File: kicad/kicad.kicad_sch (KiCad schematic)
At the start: 239 parts, among them sw1 Esc, sw10 Z, sw100 N5, sw101 N6, sw102 N2, sw103 N1, sw104 N0, sw105 MPlay, sw106 MFwd, sw107 NSlash, sw108 NStar, sw109 N8, sw11 LCtrl, sw110 N9, sw111 NMinus, sw112 NPlus, sw113 NEnter, sw114 N3, sw115 NPeriod, sw12 LSys, sw13 F2, sw14 F3, sw15 2, sw16 3, sw17 W, sw18 E, sw19 S, sw2 F1, sw20 D, sw21 X, sw22 C, sw23 LAlt, sw24 THome, sw25 F4, sw26 F5, sw27 4, sw28 5, sw29 R, sw3 Tilda, sw30 T, sw31 F, sw32 G, sw33 V, sw34 B, sw35 LSpace, sw36 TLeft, sw37 F6, sw38 F7, sw39 6, sw4 1, sw40 7, sw41 Y, sw42 U, sw43 H, sw44 J, sw45 N, sw46 M, sw47 TUp, sw48 TDown, sw49 F8, sw5 Tab, sw50 F9, sw51 8, sw52 9, sw53 I, sw54 O, sw55 K, sw56 L, sw57 Comma, sw58 Period, sw59 RSpace, sw6 Q, sw60 TRight, sw61 F10, sw62 F11, sw63 0, sw64 Minus, sw65 P, sw66 LBrack, sw67 Semi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

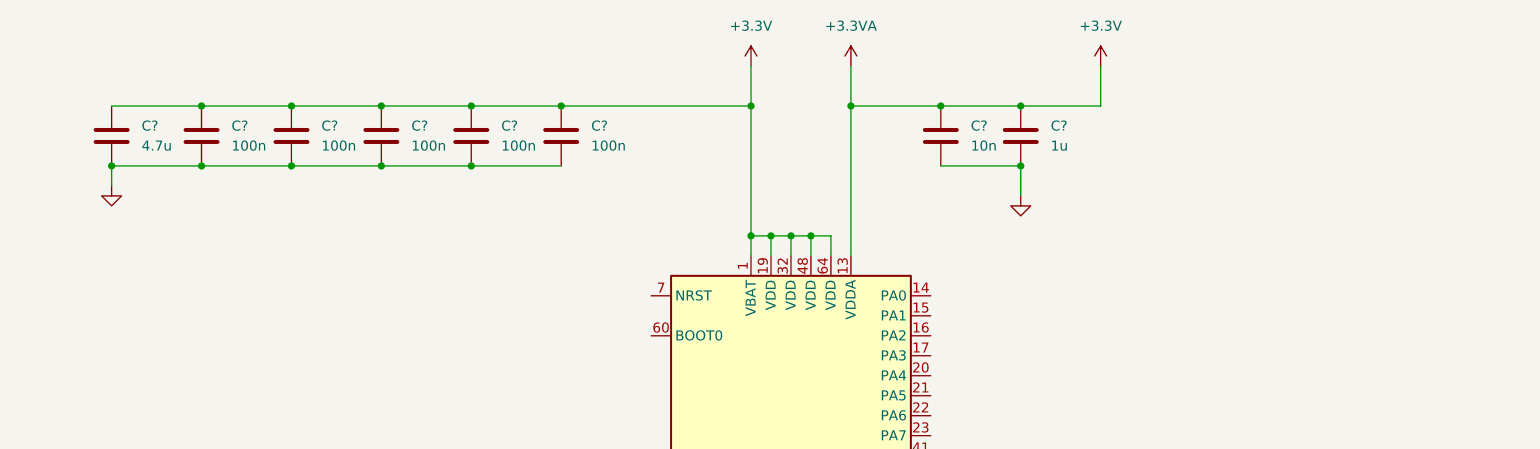
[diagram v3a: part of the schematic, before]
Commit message: Add basic voltage regulator
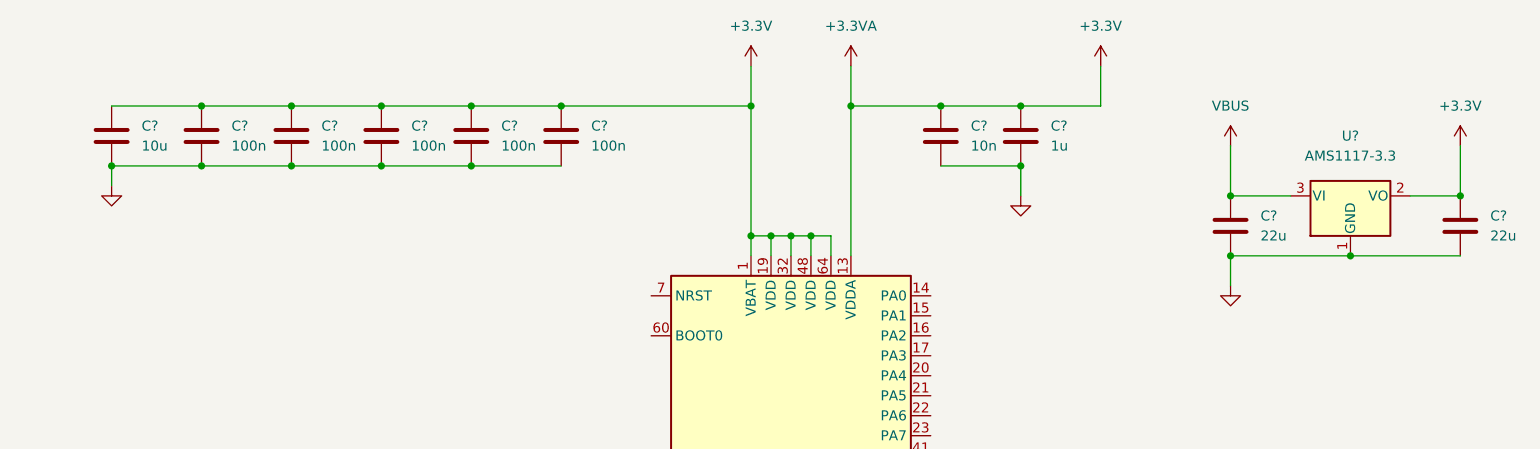
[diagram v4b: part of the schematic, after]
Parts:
- added C? (x2): 22u, symbol Device:C
- added U?: AMS1117-3.3, Package_TO_SOT_SMD:SOT-223-3_TabPin2, symbol Regulator_Linear:AMS1117-3.3
- C?: value 4.7u -> 10u
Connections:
- net +3.3V: now also C?.1, U?.2 (VO)
- net GND: now also C?.2, C?.2, U?.1 (GND)
- new net VBUS: C?.1, U?.3 (VI)
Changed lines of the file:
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@@
   (junction (at 60.96 181.61) (diameter 0) (color 0 0 0 0)
   )
+  (junction (at 397.51 52.07) (diameter 0) (color 0 0 0 0)
+  )
   (junction (at 48.26 166.37) (diameter 0) (color 0 0 0 0)
   )
@@
   (junction (at 49.53 170.18) (diameter 0) (color 0 0 0 0)
   )
+  (junction (at 368.3 52.07) (diameter 0) (color 0 0 0 0)
+  )
   (junction (at 331.47 40.64) (diameter 0) (color 0 0 0 0)
   )
@@
   (junction (at 99.06 90.17) (diameter 0) (color 0 0 0 0)
   )
+  (junction (at 368.3 59.69) (diameter 0) (color 0 0 0 0)
+  )
   (junction (at 151.13 200.66) (diameter 0) (color 0 0 0 0)
   )
@@
   (junction (at 100.33 109.22) (diameter 0) (color 0 0 0 0)
   )
+  (junction (at 383.54 59.69) (diameter 0) (color 0 0 0 0)
+  )
   (junction (at 49.53 33.02) (diameter 0) (color 0 0 0 0)
   )
@@
     (stroke (width 0) (type default) (color 0 0 0 0))
   )
+  (wire (pts (xy 397.51 52.07) (xy 397.51 45.72))
+    (stroke (width 0) (type default) (color 0 0 0 0))
+  )
   (wire (pts (xy 100.33 109.22) (xy 113.03 109.22))
     (stroke (width 0) (type default) (color 0 0 0 0))
@@
     (stroke (width 0) (type default) (color 0 0 0 0))
   )
+  (wire (pts (xy 375.92 52.07) (xy 368.3 52.07))
+    (stroke (width 0) (type default) (color 0 0 0 0))
+  )
   (wire (pts (xy 168.91 63.5) (xy 168.91 101.6))
     (stroke (width 0) (type default) (color 0 0 0 0))
   )
+  (wire (pts (xy 383.54 59.69) (xy 397.51 59.69))
+    (stroke (width 0) (type default) (color 0 0 0 0))
+  )
   (wire (pts (xy 73.66 120.65) (xy 73.66 135.89))
     (stroke (width 0) (type default) (color 0 0 0 0))
@@
     (stroke (width 0) (type default) (color 0 0 0 0))
   )
+  (wire (pts (xy 391.16 52.07) (xy 397.51 52.07))
+    (stroke (width 0) (type default) (color 0 0 0 0))
+  )
   (wire (pts (xy 100.33 196.85) (xy 99.06 196.85))
     (stroke (width 0) (type default) (color 0 0 0 0))
@@
     (stroke (width 0) (type default) (color 0 0 0 0))
   )
+  (wire (pts (xy 368.3 59.69) (xy 383.54 59.69))
+    (stroke (width 0) (type default) (color 0 0 0 0))
+  )
   (wire (pts (xy 87.63 139.7) (xy 87.63 147.32))
     (stroke (width 0) (type default) (color 0 0 0 0))
@@
     (stroke (width 0) (type default) (color 0 0 0 0))
   )
+  (wire (pts (xy 368.3 45.72) (xy 368.3 52.07))
+    (stroke (width 0) (type default) (color 0 0 0 0))
+  )
   (wire (pts (xy 60.96 181.61) (xy 60.96 196.85))
     (stroke (width 0) (type default) (color 0 0 0 0))
@@
     (stroke (width 0) (type default) (color 0 0 0 0))
   )
+  (wire (pts (xy 368.3 59.69) (xy 368.3 63.5))
+    (stroke (width 0) (type default) (color 0 0 0 0))
+  )
   (wire (pts (xy 307.34 40.64) (xy 283.21 40.64))
     (stroke (width 0) (type default) (color 0 0 0 0))
@@
     (pin "2")
   )
+  (symbol (lib_id "Regulator_Linear:AMS1117-3.3") (at 383.54 52.07 0) (unit 1)
+    (in_bom yes) (on_board yes) (fields_autoplaced)
+    (property "Reference" "U?" (id 0) (at 383.54 44.45 0))
+    (property "Value" "AMS1117-3.3" (id 1) (at 383.54 46.99 0))
+    (property "Footprint" "Package_TO_SOT_SMD:SOT-223-3_TabPin2" (id 2) (at 383.54 46.99 0)
+      (effects (font (size 1.27 1.27)) hide)
+    )
+    (property "Datasheet" "http://www.advanced-monolithic.com/pdf/ds1117.pdf" (id 3) (at 386.08 58.42 0)
+      (effects (font (size 1.27 1.27)) hide)
+    )
+    (pin "1")
+    (pin "2")
+    (pin "3")
+  )
   (symbol (lib_id "pspice:DIODE") (at 92.71 74.93 180) (unit 1)
     (in_bom yes) (on_board yes) (fields_autoplaced)
@@
     (pin "2")
   )
+  (symbol (lib_id "power:GND") (at 368.3 63.5 0) (unit 1)
+    (in_bom yes) (on_board yes) (fields_autoplaced)
+    (property "Reference" "#PWR?" (id 0) (at 368.3 69.85 0)
+      (effects (font (size 1.27 1.27)) hide)
+    )
+    (property "Value" "GND" (id 1) (at 368.3 68.58 0)
+      (effects (font (size 1.27 1.27)) hide)
+    )
+    (property "Footprint" "" (id 2) (at 368.3 63.5 0)
+      (effects (font (size 1.27 1.27)) hide)
+    )
+    (property "Datasheet" "" (id 3) (at 368.3 63.5 0)
+      (effects (font (size 1.27 1.27)) hide)
+    )
+    (pin "1")
+  )
   (symbol (lib_id "pspice:DIODE") (at 80.01 166.37 180) (unit 1)
     (in_bom yes) (on_board yes) (fields_autoplaced)
@@
     (pin "2")
   )
+  (symbol (lib_id "Device:C") (at 397.51 55.88 0) (unit 1)
+    (in_bom yes) (on_board yes) (fields_autoplaced)
+    (property "Reference" "C?" (id 0) (at 401.32 54.6099 0)
+      (effects (font (size 1.27 1.27)) (justify left))
+    )
+    (property "Value" "22u" (id 1) (at 401.32 57.1499 0)
+      (effects (font (size 1.27 1.27)) (justify left))
+    )
+    (property "Footprint" "" (id 2) (at 398.4752 59.69 0)
+      (effects (font (size 1.27 1.27)) hide)
+    )
+    (property "Datasheet" "~" (id 3) (at 397.51 55.88 0)
+      (effects (font (size 1.27 1.27)) hide)
+    )
+    (pin "1")
+    (pin "2")
+  )
   (symbol (lib_id "pspice:DIODE") (at 92.71 120.65 180) (unit 1)
     (in_bom yes) (on_board yes) (fields_autoplaced)
@@
     (pin "2")
   )
+  (symbol (lib_id "power:+3.3V") (at 397.51 45.72 0) (unit 1)
+    (in_bom yes) (on_board yes) (fields_autoplaced)
+    (property "Reference" "#PWR?" (id 0) (at 397.51 49.53 0)
+      (effects (font (size 1.27 1.27)) hide)
+    )
+    (property "Value" "+3.3V" (id 1) (at 397.51 40.64 0))
+    (property "Footprint" "" (id 2) (at 397.51 45.72 0)
+      (effects (font (size 1.27 1.27)) hide)
+    )
+    (property "Datasheet" "" (id 3) (at 397.51 45.72 0)
+      (effects (font (size 1.27 1.27)) hide)
+    )
+    (pin "1")
+  )
   (symbol (lib_id "pspice:DIODE") (at 130.81 120.65 180) (unit 1)
     (in_bom yes) (on_board yes) (fields_autoplaced)
@@
     (pin "2")
   )
+  (symbol (lib_id "Device:C") (at 368.3 55.88 0) (unit 1)
+    (in_bom yes) (on_board yes) (fields_autoplaced)
+    (property "Reference" "C?" (id 0) (at 372.11 54.6099 0)
+      (effects (font (size 1.27 1.27)) (justify left))
+    )
+    (property "Value" "22u" (id 1) (at 372.11 57.1499 0)
+      (effects (font (size 1.27 1.27)) (justify left))
+    )
+    (property "Footprint" "" (id 2) (at 369.2652 59.69 0)
+      (effects (font (size 1.27 1.27)) hide)
+    )
+    (property "Datasheet" "~" (id 3) (at 368.3 55.88 0)
+      (effects (font (size 1.27 1.27)) hide)
+    )
+    (pin "1")
+    (pin "2")
+  )
   (symbol (lib_id "pspice:DIODE") (at 130.81 166.37 180) (unit 1)
     (in_bom yes) (on_board yes) (fields_autoplaced)
@@
       (effects (font (size 1.27 1.27)) (justify left))
     )
-    (property "Value" "4.7u" (id 1) (at 229.87 45.7199 0)
+    (property "Value" "10u" (id 1) (at 229.87 45.7199 0)
       (effects (font (size 1.27 1.27)) (justify left))
     )
@@
     (pin "2")
   )
+  (symbol (lib_id "power:VBUS") (at 368.3 45.72 0) (unit 1)
+    (in_bom yes) (on_board yes) (fields_autoplaced)
+    (property "Reference" "#PWR?" (id 0) (at 368.3 49.53 0)
+      (effects (font (size 1.27 1.27)) hide)
+    )
+    (property "Value" "VBUS" (id 1) (at 368.3 40.64 0))
+    (property "Footprint" "" (id 2) (at 368.3 45.72 0)
+      (effects (font (size 1.27 1.27)) hide)
+    )
+    (property "Datasheet" "" (id 3) (at 368.3 45.72 0)
+      (effects (font (size 1.27 1.27)) hide)
+    )
+    (pin "1")
+  )
   (symbol (lib_id "power:GND") (at 307.34 157.48 0) (unit 1)
     (in_bom yes) (on_board yes) (fields_autoplaced)
@@
       (reference "#PWR?") (unit 1) (value "+3.3V") (footprint "")
     )
+    (path "/683e92a8-c8e2-4530-9b15-24ec56320700"
+      (reference "#PWR?") (unit 1) (value "GND") (footprint "")
+    )
     (path "/7bf00b94-0006-417a-8563-109264dcbb50"
       (reference "#PWR?") (unit 1) (value "GND") (footprint "")
     )
+    (path "/86041611-8dea-4aad-97c3-4ceadede0e14"
+      (reference "#PWR?") (unit 1) (value "+3.3V") (footprint "")
+    )
     (path "/c469a32f-d4ac-4add-a99b-6ec47ca9501b"
       (reference "#PWR?") (unit 1) (value "GND") (footprint "")
     )
+    (path "/f4851548-8ef8-4c6e-8b7e-0d56dc8573f6"
+      (reference "#PWR?") (unit 1) (value "VBUS") (footprint "")
+    )
     (path "/0825afc5-f175-481a-885f-eaa7a1aa509e"
       (reference "C?") (unit 1) (value "100n") (footprint "")
@@
       (reference "C?") (unit 1) (value "10n") (footprint "")
     )
+    (path "/6d41cc7f-3e1f-4a36-b744-51f7ae0f2d7a"
+      (reference "C?") (unit 1) (value "22u") (footprint "")
+    )
+    (path "/8e5724d7-f0d4-4e0f-9e4c-116a2a4992e6"
+      (reference "C?") (unit 1) (value "22u") (footprint "")
+    )
     (path "/b61eef2f-f4b6-40f6-b564-ccb91fa5d44c"
       (reference "C?") (unit 1) (value "1u") (footprint "")
     )
     (path "/b7a35a1b-5a18-4cb0-9d7a-28183d98e0e5"
-      (reference "C?") (unit 1) (value "4.7u") (footprint "")
+      (reference "C?") (unit 1) (value "10u") (footprint "")
     )
     (path "/cd51c0aa-e00e-47bc-acad-e6c81c303c58"
@@
       (reference "MCU1") (unit 1) (value "STM32F103RBTx") (footprint "Package_QFP:LQFP-64_10x10mm_P0.5mm")
     )
+    (path "/29726719-b43f-4dd8-a857-dd2f5c3cb269"
+      (reference "U?") (unit 1) (value "AMS1117-3.3") (footprint "Package_TO_SOT_SMD:SOT-223-3_TabPin2")
+    )
     (path "/081de0b4-74e7-403b-ae97-64bb5be841f3"

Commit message: Ground NRST and BOOT0. Delete old auto generated backup files. Don't use 'git add .' when committing...
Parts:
- added C?: 100n, symbol Device:C
- added R?: 10k, symbol Device:R
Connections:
- net GND: now also C?.2, R?.1
- net at MCU1.60 (BOOT0): now also R?.2
- net NRST: now reaches MCU1.7 (NRST)
- net NRST: now also C?.1
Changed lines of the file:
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@@
     (stroke (width 0) (type default) (color 0 0 0 0))
   )
+  (wire (pts (xy 294.64 57.15) (xy 270.51 57.15))
+    (stroke (width 0) (type default) (color 0 0 0 0))
+  )
   (wire (pts (xy 100.33 196.85) (xy 99.06 196.85))
     (stroke (width 0) (type default) (color 0 0 0 0))
@@
     (stroke (width 0) (type default) (color 0 0 0 0))
   )
+  (wire (pts (xy 283.21 69.85) (xy 280.67 69.85))
+    (stroke (width 0) (type default) (color 0 0 0 0))
+  )
   (wire (pts (xy 62.23 212.09) (xy 60.96 212.09))
     (stroke (width 0) (type default) (color 0 0 0 0))
@@
     (stroke (width 0) (type default) (color 0 0 0 0))
   )
+  (wire (pts (xy 280.67 69.85) (xy 280.67 71.12))
+    (stroke (width 0) (type default) (color 0 0 0 0))
+  )
   (wire (pts (xy 49.53 90.17) (xy 48.26 90.17))
     (stroke (width 0) (type default) (color 0 0 0 0))
@@
     (stroke (width 0) (type default) (color 0 0 0 0))
   )
+  (wire (pts (xy 294.64 64.77) (xy 294.64 57.15))
+    (stroke (width 0) (type default) (color 0 0 0 0))
+  )
   (wire (pts (xy 113.03 33.02) (xy 113.03 40.64))
     (stroke (width 0) (type default) (color 0 0 0 0))
@@
     (stroke (width 0) (type default) (color 0 0 0 0))
   )
+  (wire (pts (xy 290.83 69.85) (xy 294.64 69.85))
+    (stroke (width 0) (type default) (color 0 0 0 0))
+  )
   (wire (pts (xy 113.03 185.42) (xy 113.03 193.04))
     (stroke (width 0) (type default) (color 0 0 0 0))
@@
     (stroke (width 0) (type default) (color 0 0 0 0))
   )
+  (label "NRST" (at 270.51 57.15 0)
+    (effects (font (size 1.27 1.27)) (justify left bottom))
+  )
   (symbol (lib_id "pspice:DIODE") (at 54.61 105.41 180) (unit 1)
     (in_bom yes) (on_board yes) (fields_autoplaced)
@@
     (pin "2")
   )
+  (symbol (lib_id "Device:C") (at 270.51 60.96 0) (unit 1)
+    (in_bom yes) (on_board yes) (fields_autoplaced)
+    (property "Reference" "C?" (id 0) (at 274.32 59.6899 0)
+      (effects (font (size 1.27 1.27)) (justify left))
+    )
+    (property "Value" "100n" (id 1) (at 274.32 62.2299 0)
+      (effects (font (size 1.27 1.27)) (justify left))
+    )
+    (property "Footprint" "" (id 2) (at 271.4752 64.77 0)
+      (effects (font (size 1.27 1.27)) hide)
+    )
+    (property "Datasheet" "~" (id 3) (at 270.51 60.96 0)
+      (effects (font (size 1.27 1.27)) hide)
+    )
+    (pin "1")
+    (pin "2")
+  )
   (symbol (lib_id "Switch:SW_Push") (at 54.61 177.8 0) (unit 1)
     (in_bom yes) (on_board yes) (fields_autoplaced)
@@
     (pin "2")
   )
+  (symbol (lib_id "power:GND") (at 270.51 64.77 0) (unit 1)
+    (in_bom yes) (on_board yes) (fields_autoplaced)
+    (property "Reference" "#PWR?" (id 0) (at 270.51 71.12 0)
+      (effects (font (size 1.27 1.27)) hide)
+    )
+    (property "Value" "GND" (id 1) (at 270.51 69.85 0)
+      (effects (font (size 1.27 1.27)) hide)
+    )
+    (property "Footprint" "" (id 2) (at 270.51 64.77 0)
+      (effects (font (size 1.27 1.27)) hide)
+    )
+    (property "Datasheet" "" (id 3) (at 270.51 64.77 0)
+      (effects (font (size 1.27 1.27)) hide)
+    )
+    (pin "1")
+  )
   (symbol (lib_id "power:+3.3V") (at 307.34 35.56 0) (unit 1)
     (in_bom yes) (on_board yes) (fields_autoplaced)
@@
     (pin "2")
   )
+  (symbol (lib_id "Device:R") (at 287.02 69.85 90) (unit 1)
+    (in_bom yes) (on_board yes)
+    (property "Reference" "R?" (id 0) (at 287.02 67.31 90))
+    (property "Value" "10k" (id 1) (at 287.02 72.39 90))
+    (property "Footprint" "" (id 2) (at 287.02 71.628 90)
+      (effects (font (size 1.27 1.27)) hide)
+    )
+    (property "Datasheet" "~" (id 3) (at 287.02 69.85 0)
+      (effects (font (size 1.27 1.27)) hide)
+    )
+    (pin "1")
+    (pin "2")
+  )
   (symbol (lib_id "pspice:DIODE") (at 156.21 74.93 180) (unit 1)
     (in_bom yes) (on_board yes) (fields_autoplaced)
@@
     (pin "2")
   )
+  (symbol (lib_id "power:GND") (at 280.67 71.12 0) (unit 1)
+    (in_bom yes) (on_board yes) (fields_autoplaced)
+    (property "Reference" "#PWR?" (id 0) (at 280.67 77.47 0)
+      (effects (font (size 1.27 1.27)) hide)
+    )
+    (property "Value" "GND" (id 1) (at 280.67 76.2 0)
+      (effects (font (size 1.27 1.27)) hide)
+    )
+    (property "Footprint" "" (id 2) (at 280.67 71.12 0)
+      (effects (font (size 1.27 1.27)) hide)
+    )
+    (property "Datasheet" "" (id 3) (at 280.67 71.12 0)
+      (effects (font (size 1.27 1.27)) hide)
+    )
+    (pin "1")
+  )
   (symbol (lib_id "Switch:SW_Push") (at 143.51 147.32 0) (unit 1)
     (in_bom yes) (on_board yes) (fields_autoplaced)
@@
       (reference "#PWR0102") (unit 1) (value "+3.3V") (footprint "")
     )
+    (path "/3e78621f-57d4-401a-bbaa-9fece569d4f3"
+      (reference "#PWR?") (unit 1) (value "GND") (footprint "")
+    )
     (path "/52330899-ee7c-4106-8987-9aa3b8de3a9a"
       (reference "#PWR?") (unit 1) (value "+3.3VA") (footprint "")
@@
       (reference "#PWR?") (unit 1) (value "GND") (footprint "")
     )
+    (path "/e80b6365-16f3-438c-b7a8-de64f31f3d3c"
+      (reference "#PWR?") (unit 1) (value "GND") (footprint "")
+    )
     (path "/f4851548-8ef8-4c6e-8b7e-0d56dc8573f6"
       (reference "#PWR?") (unit 1) (value "VBUS") (footprint "")
@@
       (reference "C?") (unit 1) (value "100n") (footprint "")
     )
+    (path "/2e9f915f-a2a5-44b6-92ff-3c25fe6af4bf"
+      (reference "C?") (unit 1) (value "100n") (footprint "")
+    )
     (path "/3e4a6ec9-5489-4310-830c-7c5193bba267"
       (reference "C?") (unit 1) (value "10n") (footprint "")
@@
       (reference "MCU1") (unit 1) (value "STM32F103RBTx") (footprint "Package_QFP:LQFP-64_10x10mm_P0.5mm")
     )
+    (path "/9d8f6f81-b744-496a-be4f-21acd50b632a"
+      (reference "R?") (unit 1) (value "10k") (footprint "")
+    )
     (path "/29726719-b43f-4dd8-a857-dd2f5c3cb269"
